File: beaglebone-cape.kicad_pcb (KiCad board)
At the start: 2 copper layers, 56 parts, among them P1 BEAGLEBONE_BLACK, P2 12V, P3 RED_LIGHT, P4 JUMPERS, P5 GREEN_LIGHT, P6 CONN_01X05, P7 NC/NO JUMPER, P8 NC/NO JUMPER, P9 DOOR STRIKE/MAGNET, Q1 2N7000, Q2 2N7000, Q3 2N7000, Q4 2N7000, SW1 PWR_SWITCH, SW2 RESET_SWITCH, U1 24C256, U2 V7805-2000, U3 4N25, U4 4N25

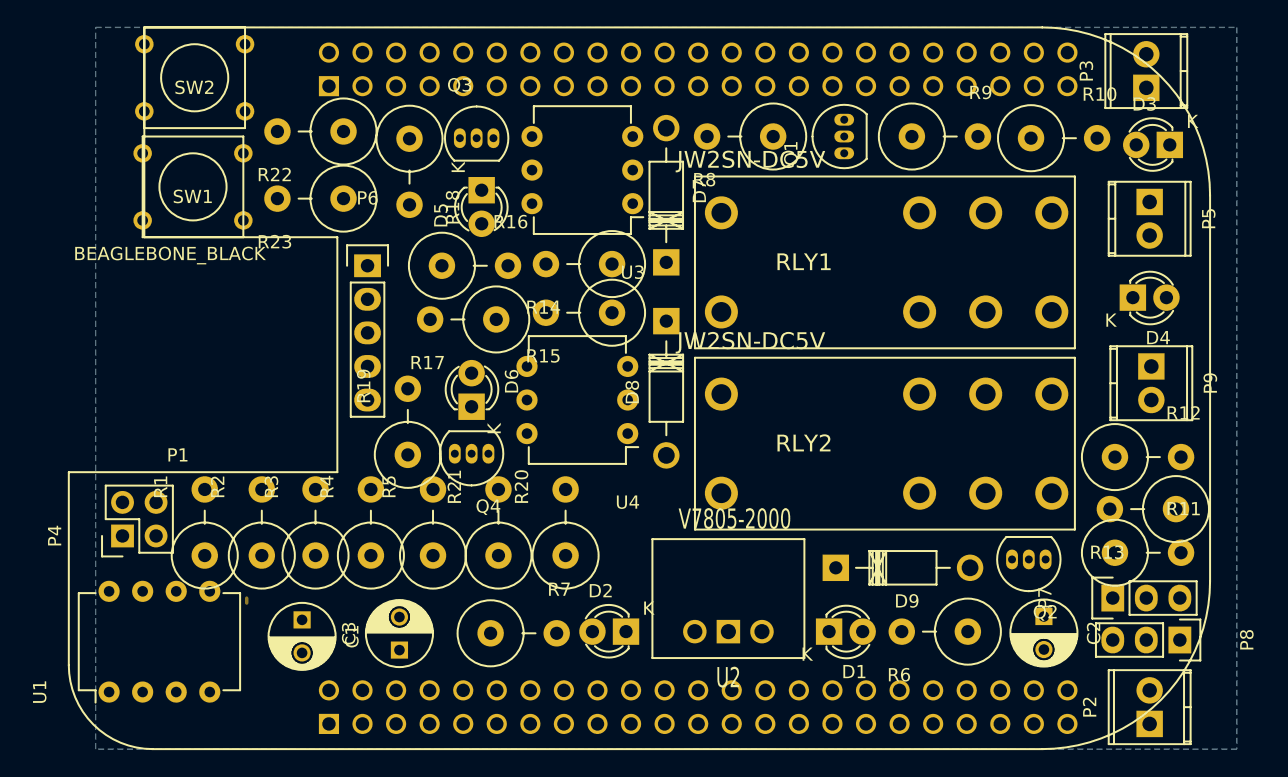
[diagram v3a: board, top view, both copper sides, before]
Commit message: tweaking of component placement on board
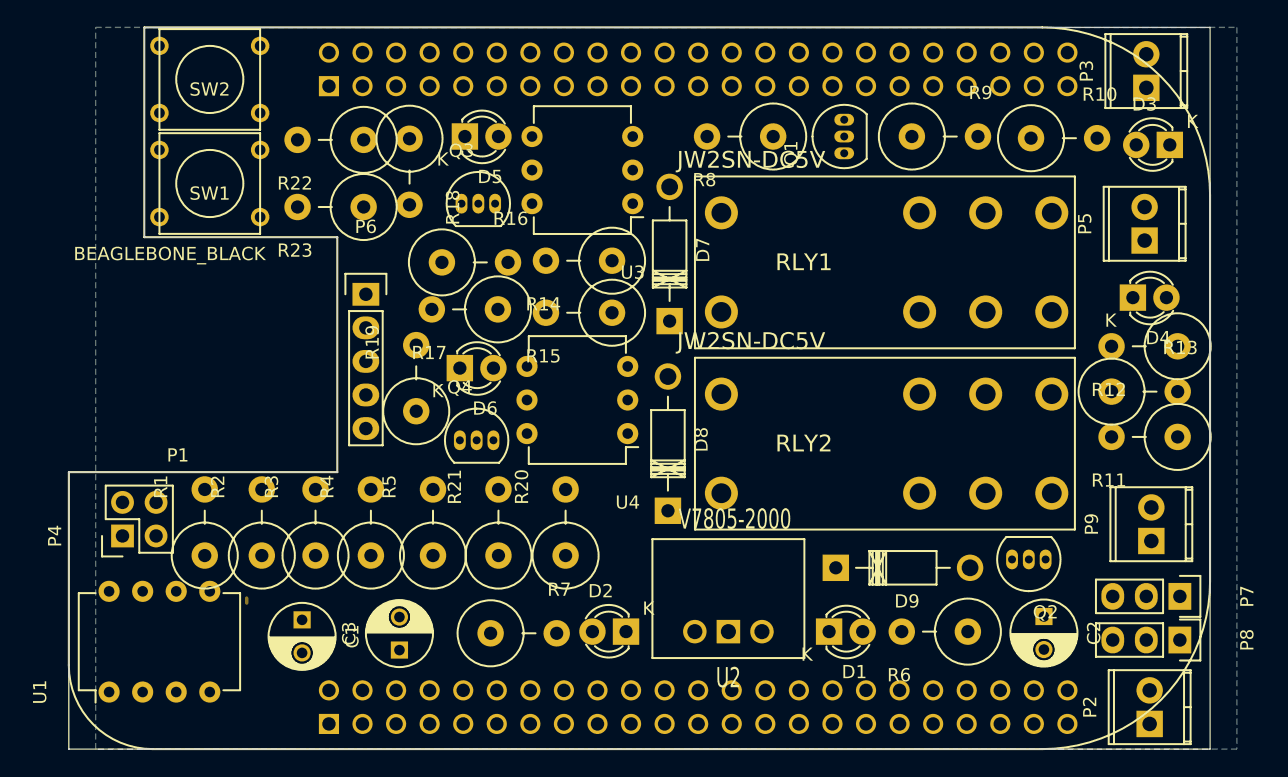
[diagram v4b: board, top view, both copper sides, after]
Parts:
- moved D8 14.4 mm to (139.8, 121.7), turned to 90 degrees
- moved P9 13.2 mm to (176.4, 124.0), turned to 90 degrees
- moved R13 8.89 mm to (175.9, 112.6), turned to 0 degrees
- moved R11 8.77 mm to (175.9, 116.1), turned to 180 degrees
- moved R12 8.39 mm to (175.9, 109.2), turned to 180 degrees
- moved P7 5.08 mm to (178.6, 128.1), turned to 270 degrees
- moved Q3 4.95 mm to (124.2, 98.4)
- moved D7 4.45 mm to (140.0, 107.3)
- moved D5 4.26 mm to (124.5, 93.3), turned to 0 degrees
- moved R19 3.36 mm to (120.8, 111.6)
- moved D6 3.05 mm to (124.1, 110.9), turned to 0 degrees
- moved P5 2.95 mm to (175.9, 101.2), turned to 90 degrees
- moved Q4 2.39 mm to (124.1, 116.3), turned to 0 degrees
- moved P6 2.16 mm to (117.0, 105.3)
- moved R22 1.65 mm to (114.3, 93.6)
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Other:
- board outline added: 86.4 x 54.6 mm

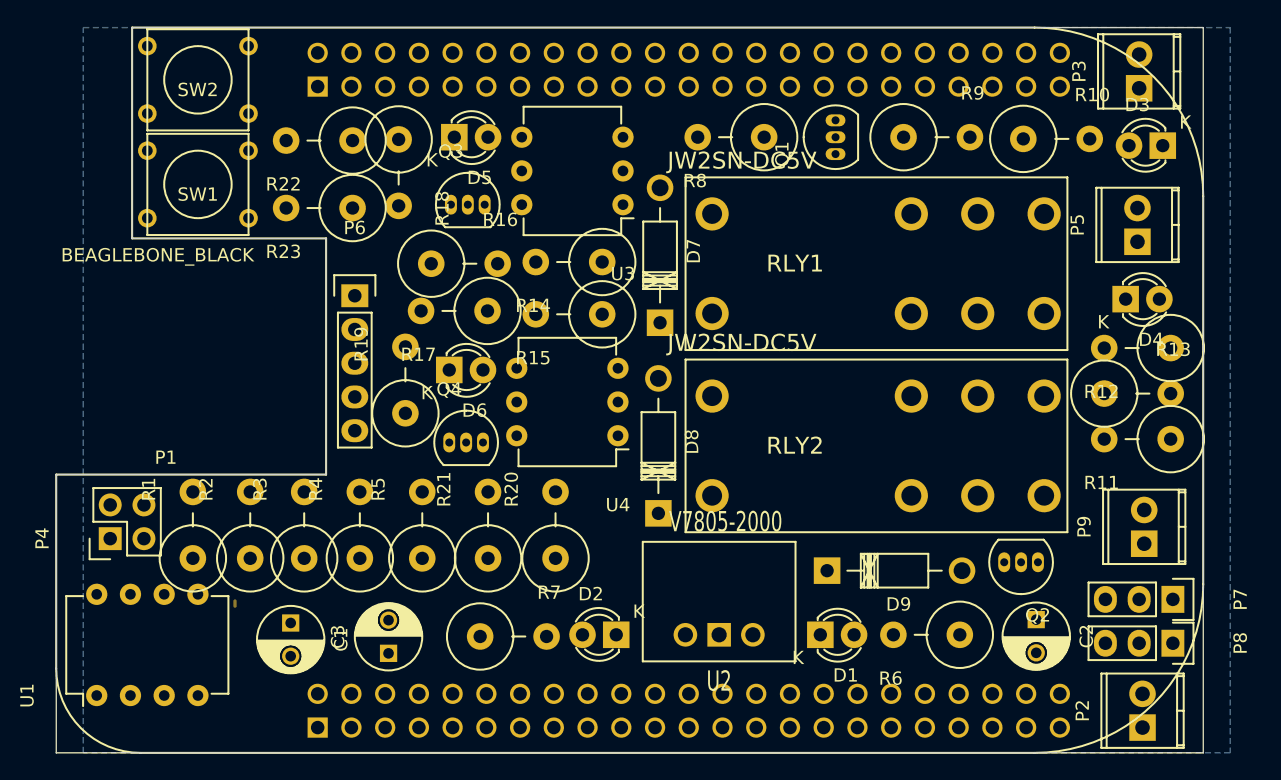
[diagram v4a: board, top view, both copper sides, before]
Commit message: Finished 90% of traces and no ground planes yet
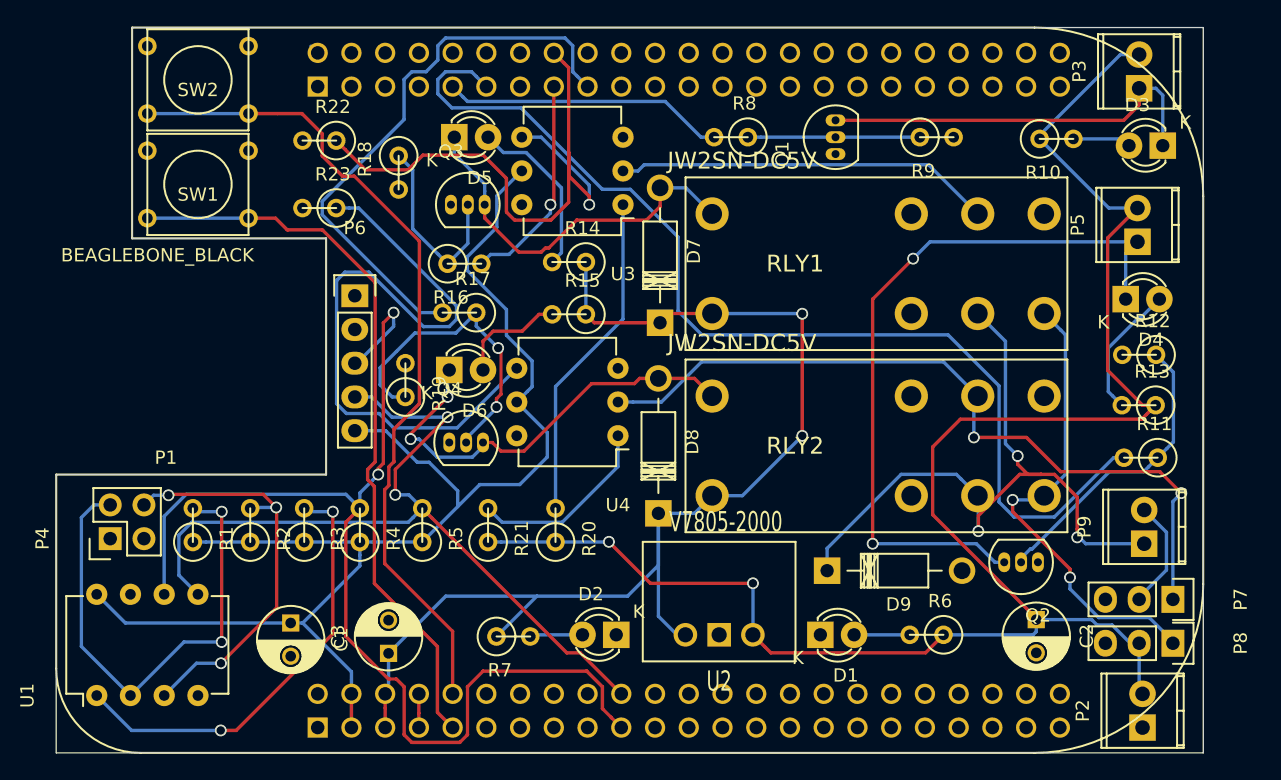
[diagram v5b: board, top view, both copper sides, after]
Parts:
- R1, R10, R11, R12, R13, R14, R15, R16, R17, R18, R19, R2, R20, R21, R22, R23, R3, R4, R5, R6, R7, R8, R9: footprint Resistors_ThroughHole:Resistor_Vertical_RM5mm -> Discret:R1
- moved R11 1.42 mm to (176.1, 117.5)
- moved R13 0.88 mm to (176.0, 113.5), turned to 180 degrees
- moved R12 0.52 mm to (176.0, 109.7)
- moved R17 0.40 mm to (124.8, 106.6)
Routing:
- net +12V: track 0.00 -> 133.0 mm, vias 0 -> 2
- net +3V3: track 0.00 -> 100.5 mm
- net +5V: track 0.00 -> 90.6 mm, vias 0 -> 2
- net /I2C2_SCL: track 0.00 -> 85.9 mm, vias 0 -> 2
- net /GPIO_45: track 0.00 -> 80.5 mm
- net /SYS_RESETn: track 0.00 -> 62.9 mm
- net /I2C2_SDA: track 0.00 -> 62.5 mm, vias 0 -> 2
- net Net-(P7-Pad1): track 0.00 -> 58.3 mm, vias 0 -> 2
- net /PWR_BUT: track 0.00 -> 55.5 mm
- net Net-(D4-Pad1): track 0.00 -> 55.3 mm, vias 0 -> 2
- net Net-(D9-Pad1): track 0.00 -> 52.3 mm, vias 0 -> 3
- net /LOCK_RELAYS/R2_READ: track 0.00 -> 49.9 mm
- net /LOCK_RELAYS/R1_READ: track 0.00 -> 47.3 mm, vias 0 -> 1
- net /LOCK_RELAYS/R2_ENGAGE: track 0.00 -> 43.2 mm
- net /A1: track 0.00 -> 38.2 mm, vias 0 -> 2
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- removed copper zone on B.Cu, net GND
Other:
- net class +12V PWR added: clearance 0.2286, trace_width 0.254, via_dia 0.889, via_drill 0.635
- net class +5V PWR added: clearance 0.2286, trace_width 0.254, via_dia 0.889, via_drill 0.635

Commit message: lines all connected, need to connect ground pins
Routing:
- net Net-(P8-Pad3): track 0.00 -> 36.6 mm
- net /LOCK_RELAYS/R2_READ: track 49.9 -> 78.4 mm, vias 0 -> 2
- net Net-(D5-Pad1): track 28.9 -> 34.4 mm
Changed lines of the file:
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@@
   (general
     (links 128)
-    (no_connects 41)
-    (area 91.1624 83.064447 184.6656 140.1786)
+    (no_connects 38)
+    (area 94.437999 85.039999 180.898001 139.750001)
     (thickness 1.6)
     (drawings 8)
-    (tracks 498)
+    (tracks 521)
     (zones 0)
     (modules 56)
@@
   (segment (start 173.697899 112.501679) (end 174.023021 112.826801) (width 0.254) (layer Bottom) (net 16))
   (segment (start 174.023021 112.826801) (end 174.72152 113.5253) (width 0.254) (layer Bottom) (net 16))
+  (segment (start 126.746 98.72599) (end 126.746 98.425) (width 0.254) (layer Top) (net 17))
+  (segment (start 129.53695 105.448102) (end 128.80339 104.714542) (width 0.254) (layer Top) (net 17))
+  (segment (start 130.680968 105.448102) (end 129.53695 105.448102) (width 0.254) (layer Top) (net 17))
+  (segment (start 133.181615 101.688899) (end 133.181615 102.947455) (width 0.254) (layer Top) (net 17))
+  (segment (start 139.95146 98.568492) (end 136.831053 101.688899) (width 0.254) (layer Top) (net 17))
+  (segment (start 133.181615 102.947455) (end 130.680968 105.448102) (width 0.254) (layer Top) (net 17))
   (segment (start 139.95146 97.155) (end 139.95146 98.568492) (width 0.254) (layer Top) (net 17))
-  (segment (start 131.015217 101.993713) (end 129.310143 101.993713) (width 0.254) (layer Top) (net 17))
-  (segment (start 129.310143 101.993713) (end 126.746 99.42957) (width 0.254) (layer Top) (net 17))
-  (segment (start 139.95146 98.568492) (end 138.939351 99.580601) (width 0.254) (layer Top) (net 17))
-  (segment (start 133.680066 99.580601) (end 131.571768 101.688899) (width 0.254) (layer Top) (net 17))
-  (segment (start 131.571768 101.688899) (end 131.320031 101.688899) (width 0.254) (layer Top) (net 17))
-  (segment (start 126.746 99.42957) (end 126.746 98.425) (width 0.254) (layer Top) (net 17))
-  (segment (start 131.320031 101.688899) (end 131.015217 101.993713) (width 0.254) (layer Top) (net 17))
-  (segment (start 138.939351 99.580601) (end 133.680066 99.580601) (width 0.254) (layer Top) (net 17))
+  (segment (start 128.80339 100.78338) (end 126.746 98.72599) (width 0.254) (layer Top) (net 17))
+  (segment (start 128.80339 104.714542) (end 128.80339 100.78338) (width 0.254) (layer Top) (net 17))
+  (segment (start 136.831053 101.688899) (end 133.181615 101.688899) (width 0.254) (layer Top) (net 17))
   (segment (start 124.46 93.345) (end 124.46 94.599) (width 0.254) (layer Bottom) (net 17))
   (segment (start 124.46 94.599) (end 126.746 96.885) (width 0.254) (layer Bottom) (net 17))
@@
   (segment (start 123.215399 87.531449) (end 123.215399 86.458551) (width 0.254) (layer Bottom) (net 36))
   (segment (start 122.329449 88.417399) (end 123.215399 87.531449) (width 0.254) (layer Bottom) (net 36))
+  (segment (start 131.064 108.839) (end 129.159 110.744) (width 0.254) (layer Top) (net 37))
+  (segment (start 129.921 106.299) (end 129.921 107.696) (width 0.254) (layer Bottom) (net 37))
+  (segment (start 129.921 107.696) (end 131.064 108.839) (width 0.254) (layer Bottom) (net 37))
+  (via (at 131.064 108.839) (size 0.889) (drill 0.635) (layers Top Bottom) (net 37))
+  (segment (start 129.921 104.648) (end 129.921 106.299) (width 0.254) (layer Bottom) (net 37))
+  (via (at 129.921 104.648) (size 0.889) (drill 0.635) (layers Top Bottom) (net 37))
+  (segment (start 129.921 103.08793) (end 129.921 104.648) (width 0.254) (layer Top) (net 37))
+  (segment (start 135.610601 98.577399) (end 132.499101 101.688899) (width 0.254) (layer Top) (net 37))
+  (segment (start 132.499101 101.688899) (end 131.320031 101.688899) (width 0.254) (layer Top) (net 37))
+  (segment (start 131.320031 101.688899) (end 129.921 103.08793) (width 0.254) (layer Top) (net 37))
+  (segment (start 135.610601 88.112601) (end 135.610601 98.577399) (width 0.254) (layer Top) (net 37))
+  (segment (start 134.493 86.995) (end 135.610601 88.112601) (width 0.254) (layer Top) (net 37))
   (segment (start 129.159 110.744) (end 124.67718 115.22582) (width 0.254) (layer Bottom) (net 37))
   (segment (start 116.334988 114.147611) (end 115.59539 113.408013) (width 0.254) (layer Bottom) (net 37))
@@
   (segment (start 170.474601 108.225601) (end 170.118999 107.869999) (width 0.254) (layer Bottom) (net 101))
   (segment (start 170.118999 107.869999) (end 168.869 106.62) (width 0.254) (layer Bottom) (net 101))
+  (segment (start 158.869 120.336) (end 158.869 124.24929) (width 0.254) (layer Top) (net 102))
+  (segment (start 165.781109 131.161399) (end 172.080799 131.161399) (width 0.254) (layer Top) (net 102))
+  (segment (start 172.080799 131.161399) (end 172.3644 131.445) (width 0.254) (layer Top) (net 102))
+  (segment (start 158.869 124.24929) (end 165.781109 131.161399) (width 0.254) (layer Top) (net 102))
+  (segment (start 172.3644 131.445) (end 173.482 131.445) (width 0.254) (layer Top) (net 102))
+  (segment (start 158.869 120.336) (end 158.869 118.568234) (width 0.254) (layer Top) (net 102))
+  (segment (start 157.619001 107.869999) (end 158.869 106.62) (width 0.254) (layer Top) (net 102))
+  (segment (start 158.869 118.568234) (end 157.263399 116.962633) (width 0.254) (layer Top) (net 102))
+  (segment (start 157.263399 116.962633) (end 157.263399 108.225601) (width 0.254) (layer Top) (net 102))
+  (segment (start 157.263399 108.225601) (end 157.619001 107.869999) (width 0.254) (layer Top) (net 102))
   (segment (start 153.162 93.345) (end 159.512 93.345) (width 0.254) (layer Bottom) (net 103))
   (segment (start 146.558 93.345) (end 147.545828 93.345) (width 0.254) (layer Bottom) (net 103))
